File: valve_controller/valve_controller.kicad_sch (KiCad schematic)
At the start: 35 parts, among them J1 CDM1204-04A-FP-F9-67, J2 T4141L12041-000, J3 CDM1204-04A-FP-F9-67, P1 USB_C_Plug_USB2.0, SW1 TS09-63-25-WT-160-SMT-TR, SW2 TS09-63-25-WT-160-SMT-TR, U1 LAN8720A, U2 ADS1115IDGS, U3 MCP4728, U5 LM2596S-5, U6 LDO-LM7805MPX/NOPB, U7 ESP32-S3, U8 TVS-SMDB03CE3, Y2 ASE-25.000MHZ-LC-T

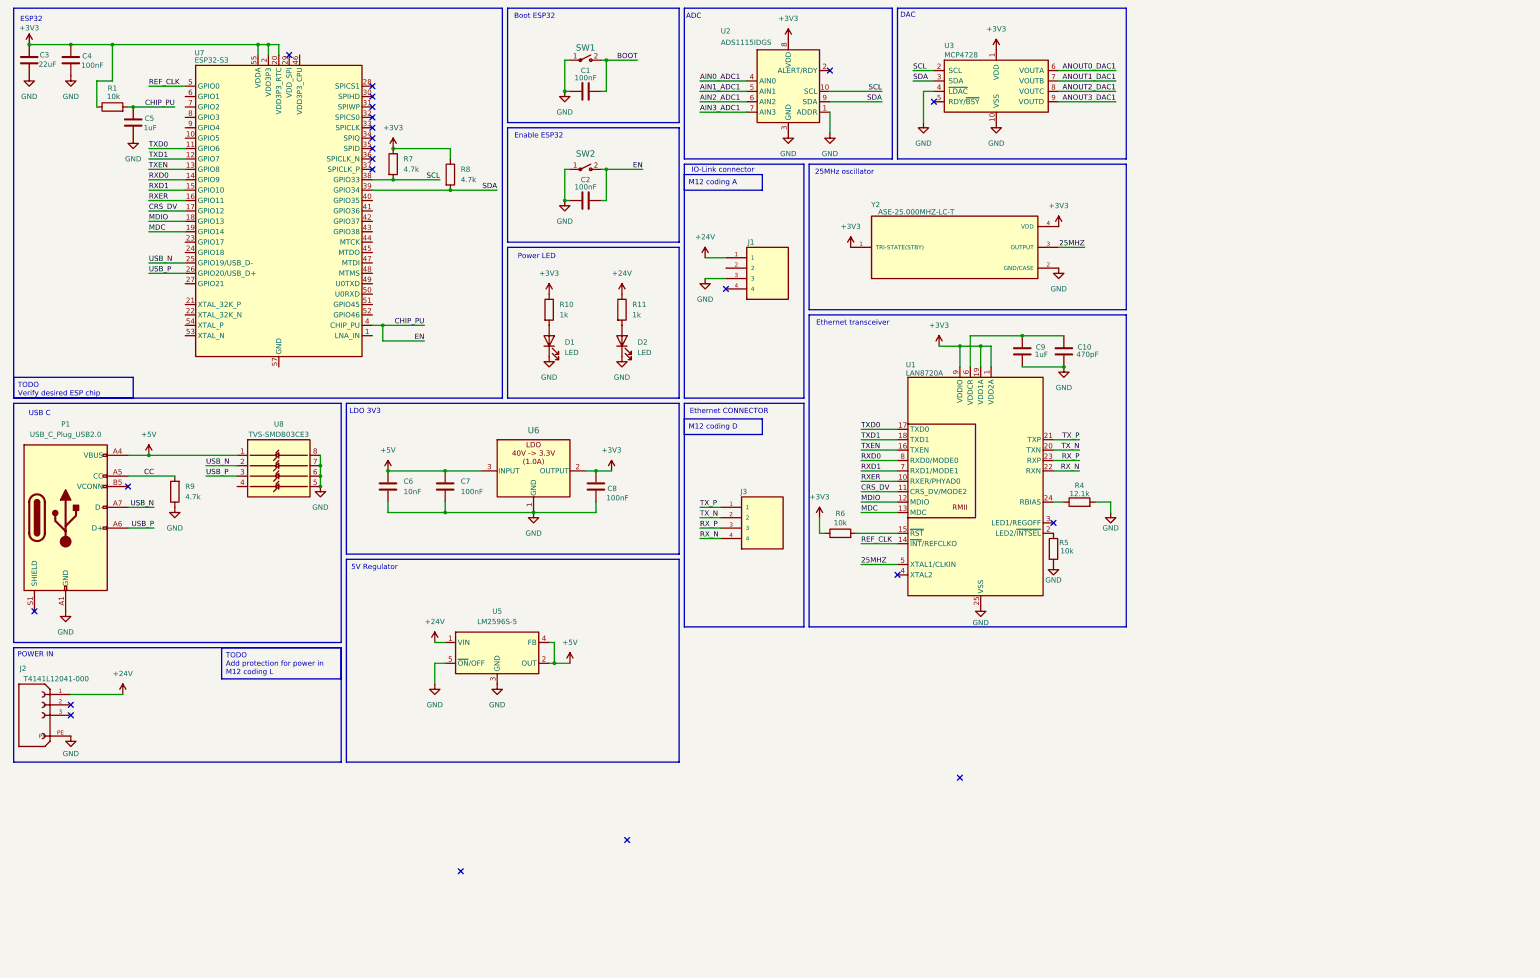
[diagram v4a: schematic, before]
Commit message: Updated + ports
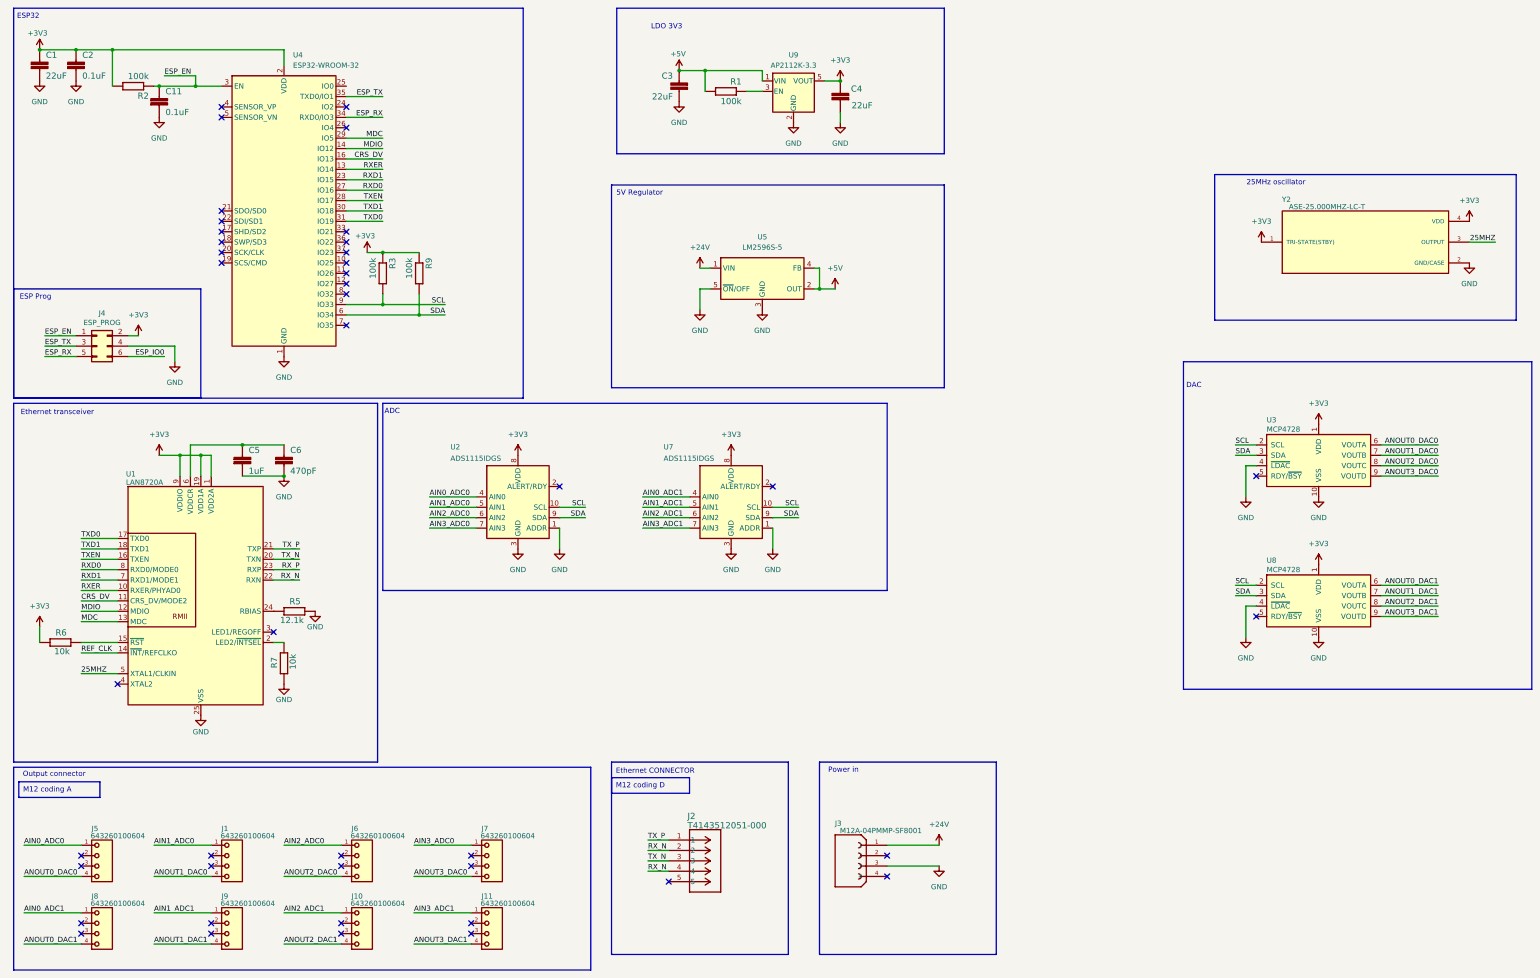
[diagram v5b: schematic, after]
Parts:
- removed C1, C2: 100nF, Capacitor_SMD:C_0805_2012Metric_Pad1.18x1.45mm_HandSolder, symbol 0_RoverLibrary:C-100nF
- removed C10: 470pF, symbol Device:C
- removed C3: 22uF, symbol Device:C
- removed C4, C7, C8: 100nF, symbol Device:C
- removed C5, C9: 1uF, symbol Device:C
- removed C6: 10nF, symbol Device:C
- removed D1, D2: LED, LED_SMD:LED_0805_2012Metric_Pad1.15x1.40mm_HandSolder, symbol RoverLibrary:LED
- removed J1, J3: CDM1204-04A-FP-F9-67, CDM1204-04A-FP-F9-67:CUI_CDM1204-04A-FP-F9-67, symbol CDM1204-04A-FP-F9-67:CDM1204-04A-FP-F9-67
- removed J2: T4141L12041-000, T4141L12041-000:TE_T4141L12041-000, symbol T4141L12041-000:T4141L12041-000
- removed P1: USB_C_Plug_USB2.0, symbol Connector:USB_C_Plug_USB2.0
- removed R1, R5, R6: 10k, symbol Device:R
- removed R10, R11: 1k, Resistor_SMD:R_0201_0603Metric, symbol Device:R
- removed R4: 12.1k, symbol Device:R
- removed R7, R8, R9: 4.7k, symbol Device:R
- removed SW1, SW2: TS09-63-25-WT-160-SMT-TR, Button_Switch_SMD:SW_DIP_SPSTx01_Slide_6.7x4.1mm_W8.61mm_P2.54mm_LowProfile, symbol 0_RoverLibrary:PushButton-TS09-63-25-WT-160-SMT-TR
- removed U6: LDO-LM7805MPX/NOPB, Package_TO_SOT_SMD:TO-252-2, symbol RoverLibrary:LDO-TLE4284DV33ATMA1
- removed U7: ESP32-S3, Package_DFN_QFN:QFN-56-1EP_7x7mm_P0.4mm_EP4x4mm, symbol MCU_Espressif:ESP32-S3
- removed U8: TVS-SMDB03CE3, Package_SO:SOIC-8_3.9x4.9mm_P1.27mm, symbol 0_RoverLibrary:TVS-SMDB03CE3/TR7TR-ND
- added C1, C3, C4: 22uF, Capacitor_SMD:C_0603_1608Metric, symbol SerialChiller-eagle-import:C-EUC1206
- added C11, C2: 0.1uF, Capacitor_SMD:C_0402_1005Metric, symbol SerialChiller-eagle-import:C-EUC0603
- added C5: 1uF, Capacitor_SMD:C_0603_1608Metric, symbol SerialChiller-eagle-import:C-EUC1206
- added C6: 470pF, Capacitor_SMD:C_0603_1608Metric, symbol SerialChiller-eagle-import:C-EUC1206
- added J1, J10, J11, J5, J6, J7, J8, J9: 643260100604, 643260100604:643260100604, symbol 643260100604:643260100604
- added J2: T4143512051-000, CONN5_T4143512051, symbol 2025-06-20_15-31-17:T4143512051-000
- added J3: M12A-04PMMP-SF8001, M12A-04PMMP-SF8001:AMPHENOL_M12A-04PMMP-SF8001, symbol M12A-04PMMP-SF8001:M12A-04PMMP-SF8001
- added J4: ESP_PROG, custom_footprints:ESP-PROG, symbol Connector_Generic:Conn_02x03_Odd_Even
- added R1, R2, R3, R9: 100k, Resistor_SMD:R_0603_1608Metric, symbol SerialChiller-eagle-import:R-EU_R0603
- added R5: 12.1k, Resistor_SMD:R_0603_1608Metric, symbol SerialChiller-eagle-import:R-EU_R0603
- added R6, R7: 10k, Resistor_SMD:R_0603_1608Metric, symbol SerialChiller-eagle-import:R-EU_R0603
- added U4: ESP32-WROOM-32, RF_Module:ESP32-WROOM-32, symbol RF_Module:ESP32-WROOM-32
- added U7: ADS1115IDGS, Package_SO:TSSOP-10_3x3mm_P0.5mm, symbol Analog_ADC:ADS1115IDGS
- added U8: MCP4728, Package_SO:MSOP-10_3x3mm_P0.5mm, symbol Analog_DAC:MCP4728
- added U9: AP2112K-3.3, Package_TO_SOT_SMD:SOT-23-5, symbol Regulator_Linear:AP2112K-3.3
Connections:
- net +24V: now also J3.1
- net +3V3: now also C1.1, C2.1, C4.1, J4.2 (Pin_2), R2.2, R3.1, R6.2, R9.1, U4.2 (VDD), U7.8 (VDD), U8.1 (VDD), U9.5 (VOUT)
- net +5V: now also C3.1, R1.2, U9.1 (VIN)
- net AIN0_ADC1: now also J8.1, U7.4 (AIN0); no longer U2.4 (AIN0)
- net AIN1_ADC1: now also J9.1, U7.5 (AIN1); no longer U2.5 (AIN1)
- net AIN2_ADC1: now also J10.1, U7.6 (AIN2); no longer U2.6 (AIN2)
- net AIN3_ADC1: now also J11.1, U7.7 (AIN3); no longer U2.7 (AIN3)
- net ANOUT0_DAC1: now also J8.4, U8.6 (VOUTA); no longer U3.6 (VOUTA)
- net ANOUT1_DAC1: now also J9.4, U8.7 (VOUTB); no longer U3.7 (VOUTB)
- net ANOUT2_DAC1: now also J10.4, U8.8 (VOUTC); no longer U3.8 (VOUTC)
- net ANOUT3_DAC1: now also J11.4, U8.9 (VOUTD); no longer U3.9 (VOUTD)
- net CRS_DV: now also U4.16 (IO13)
- net GND: now also C1.2, C11.2, C2.2, C3.2, C4.2, C5.2, C6.2, J3.3, J4.4 (Pin_4), R5.1, R7.2, U4.1 (GND), U4.15 (GND), U4.38 (GND), U4.39 (GND), U7.1 (ADDR), U7.3 (GND), U8.10 (VSS), U8.4 (~{LDAC}), U9.2 (GND)
- net MDC: now also U4.29 (IO5)
- net MDIO: now also U4.14 (IO12)
- net RXD0: now also U4.27 (IO16)
- net RXD1: now also U4.23 (IO15)
- net RXER: now also U4.13 (IO14)
- net RX_N: now also J2.2, J2.4
- net SCL: now also R3.2, U4.9 (IO33), U7.10 (SCL), U8.2 (SCL)
- net SDA: now also R9.2, U4.6 (IO34), U7.9 (SDA), U8.3 (SDA)
- net TXD0: now also U4.31 (IO19)
- net TXD1: now also U4.30 (IO18)
- net TXEN: now also U4.28 (IO17)
- net TX_N: now also J2.3
- net TX_P: now also J2.1
- net at U1.2 (LED2/~{INTSEL}): now also R7.1
- net at U1.24 (RBIAS): now also R5.2
- net at U1.15 (~{RST}): now also R6.1
- net at U1.6 (VDDCR): now also C5.1, C6.1
- new net: R1.1, U9.3 (EN)
- new net AIN0_ADC0: J5.1, U2.4 (AIN0)
- new net AIN1_ADC0: J1.1, U2.5 (AIN1)
- new net AIN2_ADC0: J6.1, U2.6 (AIN2)
- new net AIN3_ADC0: J7.1, U2.7 (AIN3)
- new net ANOUT0_DAC0: J5.4, U3.6 (VOUTA)
- new net ANOUT1_DAC0: J1.4, U3.7 (VOUTB)
- new net ANOUT2_DAC0: J6.4, U3.8 (VOUTC)
- new net ANOUT3_DAC0: J7.4, U3.9 (VOUTD)
- new net ESP_EN: C11.1, J4.1 (Pin_1), R2.1, U4.3 (EN)
- new net ESP_IO0: J4.6 (Pin_6)
- new net ESP_RX: J4.5 (Pin_5), U4.34 (RXD0/IO3)
- new net ESP_TX: J4.3 (Pin_3), U4.35 (TXD0/IO1)
- no-connect marks 22 -> 43
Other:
- note added: "ESP Prog"
- note added: "Output connector"
- note added: "Power in"
- note removed: "Boot ESP32"
- note removed: "Enable ESP32"
- note removed: "IO-Link connector"
- note removed: "POWER IN"
- note removed: "Power LED"
- note removed: "USB C"
- moved on the sheet: U1, U2, U3, U5, Y2

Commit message: Started pcb layout
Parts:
- added D1: WS2812B, LED_SMD:LED_WS2812B_PLCC4_5.0x5.0mm_P3.2mm, symbol LED:WS2812B
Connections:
- net +3V3: now also D1.1 (VDD)
- net +5V: no longer U5.4 (FB)
- net CRS_DV: now also U4.24 (IO2); no longer U4.16 (IO13)
- net ESP_RX: no longer U4.34 (RXD0/IO3)
- net ESP_TX: no longer U4.35 (TXD0/IO1)
- net GND: now also D1.3 (VSS)
- net MDC: no longer U4.29 (IO5)
- net MDIO: now also U4.23 (IO15); no longer U4.14 (IO12)
- net RXD0: no longer U4.27 (IO16)
- net RXD1: no longer U4.23 (IO15)
- net RXER: now also U4.26 (IO4); no longer U4.13 (IO14)
- net RX_N: no longer J2.2
- net RX_P: now also J2.2
- net SCL: now also U4.36 (IO22); no longer U4.9 (IO33)
- net SDA: now also U4.37 (IO23); no longer U4.6 (IO34)
- net TXD0: now also U4.13 (IO14); no longer U4.31 (IO19)
- net TXD1: now also U4.16 (IO13); no longer U4.30 (IO18)
- net TXEN: now also U4.14 (IO12); no longer U4.28 (IO17)
- new net RGB_LED: D1.4 (DIN)
- no-connect marks 43 -> 35
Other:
- note added: "LED"
- moved on the sheet: R3, R9

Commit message: Review 06/23
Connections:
- net +24V: now also J5.1
- net AIN0_ADC0: now also J5.4; no longer J5.1
- net ANOUT0_DAC0: now also J5.2; no longer J5.4
- net ESP_RX: now also U4.35 (TXD0/IO1)
- net ESP_TX: now also U4.34 (RXD0/IO3)
- net GND: now also J5.3
- no-connect marks 35 -> 33
